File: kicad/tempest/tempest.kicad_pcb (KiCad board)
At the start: 2 copper layers, 300 x 300 mm, 18 parts

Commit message: Draw every device at its real package size
The board maps existed to answer "which chip is at C4", and then drew a
24-pin ROM and a 20-pin LS245 as the same 14-pin outline. package_for()
read pin counts from DEVICES, which holds 20 Pong-era parts against the
112 part types the boards actually use, and silently fell back to DIP-14
for the other 92.

tools/packages.py is the pin-count table, kept separate from devices.py
on purpose: packaging needs one number for every part on every board,
while devices.py carries verified pinouts for the parts validate_nets.py
reasons about, and widening that set to satisfy a drawing would let the
extractor trust readings nothing has checked.

688 of 704 devices now size. check_packages.py re-derives 56 of the
entries from KiCAD's symbol library — comparing the highest pin number,
not the pin count, since KiCAD omits no-connects and a 7493 symbol has
ten pins on a DIP-14 — and confirms all 20 parts in DEVICES agree. The
Am2901 slices and the POKEY come from DIP-40 stated on the Battlezone
sheet; the 8316E from the drawing's note that a 2708 may be fitted
instead.

What does not size is now said out loud rather than quietly drawn at 14
pins: four descriptions recorded where the sheet gave no part number,
and the Atari 0351xx ROM/PROM numbers, which get the class default and
are listed as unverified until someone has a board in front of them.

Two things found while reading the corpus for packages, both logged in
asteroids.read.json rather than acted on. The -06 rate multiplier
resolution was recorded and never applied to the board data, and the
parts list disagrees with both readings on designators. F4/H4/J4 take
either an LS670 or an LS170, and the 19-007 pull-up network is fitted
only with the LS170 — same package either way, but a real failure mode.

Also: republishing a board without --machine used to unlink it from its
machine, because most definitions carry no machine of their own and the
link lived only in boards.json. publish_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
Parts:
- UC4, UD10: footprint DIP-14_W7.62mm -> DIP-16_W7.62mm
- UK11: footprint DIP-14_W7.62mm -> DIP-8_W7.62mm
- UM12, UN12, UR9: footprint DIP-14_W7.62mm -> DIP-20_W7.62mm

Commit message: Drop two grid rows that do not exist, and span the devices that do
Atari's grid alphabet skips G, I, O and Q, and the board definitions
listed G and Q as rows. Every device below F was therefore drawn a row
too low, the rendered board carried two empty bands, and F/H1 looked
like a three-position span for a part 1.2in long on a 0.75in pitch.

Confirmed three ways before touching it. Nothing in any read, signature
or signal record in this repo sits in a G or Q row, while both
neighbours of each are populated on the two densest boards — Battlezone
P:6 R:2, Asteroids-03 P:4 R:3. The sheets' own spanning designators
treat F and H as adjacent and H and J as adjacent, which is only
possible if G and I are not positions. And with G removed, F/H falls out
as an adjacent pair, which is what a 24-pin ROM needs. Pong predates the
convention and legitimately uses G, so it keeps its grid.

Spans are now data rather than prose. A device drawn across two or three
cells is still keyed at its first cell, because that is the only thing
`ics` may be keyed by, but the sheet's own designator goes in a `spans`
map and the footprint is placed at the mean of the cells it names. A
DIP-40 at B/C2 sits between B2 and C2 instead of hanging equally over A2
and C2. The build rejects a span whose rows are not adjacent — that
failure almost always means the grid is wrong, not the span.

Two more inconsistencies found and logged rather than guessed at. Two of
the Math Box's four Am2901 slices carry a span and two do not, though
all four are the same DIP-40 on the same pitch. And asteroids-04.json
carries five devices at the -03 PROM positions alongside the -04 ROMs
and is missing 035144-02 at D/E1, contradicting the substitution table,
memory_by_revision and its own status text in the same breath.

Co-Authored-By: Claude Opus 5 <noreply@anthropic.com>
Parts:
- moved UA4 38.1 mm to (102.2, 265.6)
- moved UA6 38.1 mm to (153.0, 265.6)
- moved UE6 38.1 mm to (153.0, 189.4)
- moved UB4 38.1 mm to (102.2, 246.6)
- moved UD10 38.1 mm to (254.6, 208.5)
- moved UD4 38.1 mm to (102.2, 208.5)
- moved UF3 38.1 mm to (76.8, 170.4)
- moved UC4 38.1 mm to (102.2, 227.6)
- moved UK11 19.1 mm to (280.0, 113.2)
- moved UK9 19.1 mm to (229.2, 113.2)
- moved UN12 19.1 mm to (305.4, 56.1)
- moved UN13 19.1 mm to (330.8, 56.1)
- moved UN6 19.1 mm to (153.0, 56.1)
- moved UL12 19.0 mm to (305.4, 94.2)
- moved UL6 19.0 mm to (153.0, 94.2)
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
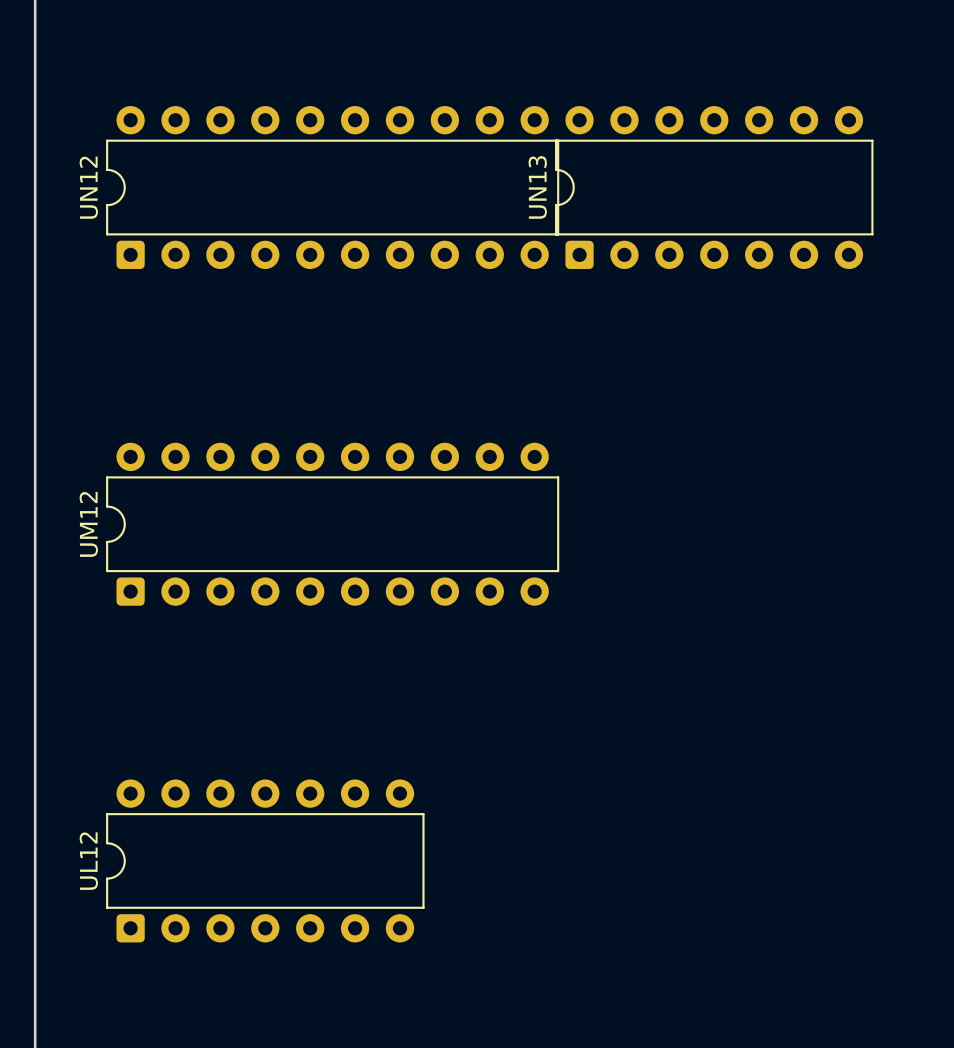
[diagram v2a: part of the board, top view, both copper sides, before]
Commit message: Name the four parts the sheets never did
C5, E12 and M12 on Asteroids were recorded by function — "counter",
"op-amp", "DIP switch" — because the drawings give no part number for
them, and they were the last devices the board maps could not size. The
parts lists give all three, and agree across printings.

C5 is a 9316. Five printings name a counter there: the 6th, 7th and
Cocktail 3rd say 37-9316, the 1st and 2nd say 37-74LS161, and the 9316
is Fairchild's 74161, so those are the same part and not a conflict. It
matches the read's own note that C5 divides 3kHz by 12 for the NMI.

E12 is Atari 137108-001, item 130, "Operational Amplifier Integrated
Circuit", at E12 in three printings; the Caberat manual names the type,
TL081CP. Same designator, same block, three documents. The same item
also lists a B/C12 location that nothing in the read accounts for, which
is noted and not acted on.

M12 is Atari 66-114P1T, a 4-station DIP switch, item 143 at M12 in three
printings. Sized as DIP-8, since n SPST switches in a DIP is 2n pins;
the 8-station switches on Battlezone and Tempest are DIP-16 for the same
reason.

All three are cross-document confirmations rather than re-readings of
the same sheet, which is the route the house rules say to try first and
the one that has resolved every conflict here so far. Every device on
every board now has a package: 106 of 106 part types, 694 of 694
devices. What remains unverified is the twenty Atari 0351xx ROM/PROM
positions, drawn on a class default, and those want a board.

Co-Authored-By: Claude Opus 5 <noreply@anthropic.com>
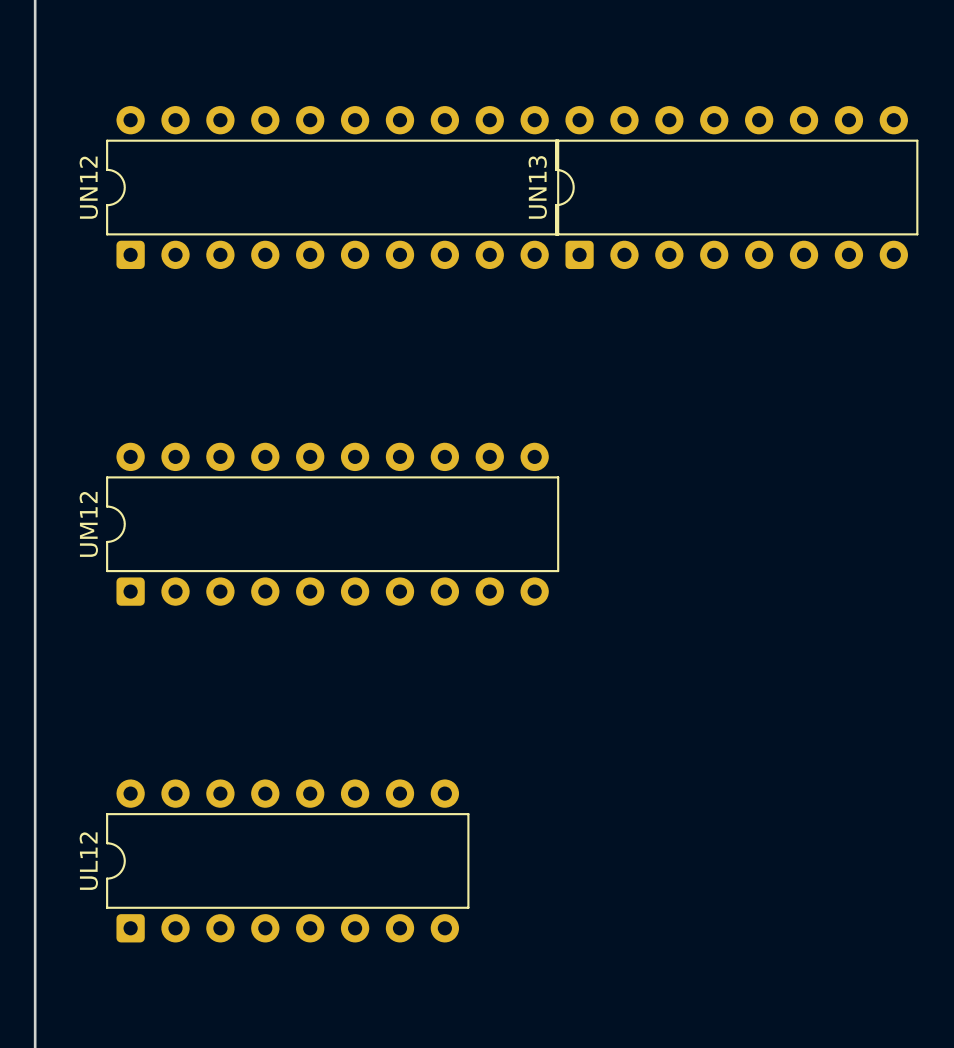
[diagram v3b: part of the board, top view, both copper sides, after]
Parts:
- UL12, UN13: footprint DIP-14_W7.62mm -> DIP-16_W7.62mm

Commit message: Unlock Centipede and Tempest on a hyphen
Checking whether mikesarcade.com had anything this corpus lacks turned
up something better: Centipede and Tempest harvested nothing at all,
from forty-six and thirty-seven documents each, while Asteroids and
Battlezone gave up eighty to a hundred designators apiece. Same
manufacturer, same era, same parts-list format.

The difference was one character. Asteroids writes 'Type 74LS04
Integrated Circuit (B5)'; Centipede and Tempest write 'Type-74LS04'. The
type pattern required whitespace, so those rows never matched, fell
through to the count layout, found no leading quantity, and were
discarded silently.

Centipede goes from 23 devices to 87, Tempest from 18 to 83. Both
agree with themselves across every printing with no split, and both
confirm every drawing device the lists also name. Tempest needs
--figure: its manual carries an Auxiliary PCB alongside the
vector-generator board, and only the latter has a map.

Two more readings resolved against the drawing, on the same evidence as
Missile Command's D3. Centipede M4 is a 74LS175, not a 74LS75 — nine
printings, and 75 against 175 is a dropped digit. Tempest L6 is a
74LS670, not a 74LS14: four printings put it in a bank of three register
files at K6, L6 and M6, which is the same trio Asteroids has at F4, H4
and J4 on the same vector generator, so the grouping is coherent as well
as attested.

74LS373 and the CD4584B join the packaging table. 1,461 devices across
27 boards, all sized, none contradicted by a socket entry.

Co-Authored-By: Claude Opus 5 <noreply@anthropic.com>
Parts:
- added UA1: 74LS244, DIP-20_W7.62mm, F.Cu at (26.0, 256.1)
- added UA7: 74LS02, DIP-14_W7.62mm, F.Cu at (178.4, 265.6)
- added UA8: 74LS109, DIP-16_W7.62mm, F.Cu at (203.8, 265.6)
- added UA9: 74LS164, DIP-14_W7.62mm, F.Cu at (229.2, 265.6)
- added UB1: 74LS244, DIP-20_W7.62mm, F.Cu at (26.0, 237.1)
- added UB3: 74LS139, DIP-16_W7.62mm, F.Cu at (76.8, 246.6)
- added UB5: 74LS02, DIP-14_W7.62mm, F.Cu at (127.6, 246.6)
- added UB6: 74LS27, DIP-14_W7.62mm, F.Cu at (153.0, 246.6)
- added UB7: 74S74, DIP-14_W7.62mm, F.Cu at (178.4, 246.6)
- added UB8: 74LS74, DIP-14_W7.62mm, F.Cu at (203.8, 246.6)
- added UB9: 74LS32, DIP-14_W7.62mm, F.Cu at (229.2, 246.6)
- added UC1: 74LS139, DIP-16_W7.62mm, F.Cu at (26.0, 227.6)
- added UC3: 74LS32, DIP-14_W7.62mm, F.Cu at (76.8, 227.6)
- added UC5: 74S260, DIP-14_W7.62mm, F.Cu at (127.6, 227.6)
- added UC6: 74S02, DIP-14_W7.62mm, F.Cu at (153.0, 227.6)
- added UC7: 74S74, DIP-14_W7.62mm, F.Cu at (178.4, 227.6)
- added UC8: 74LS161, DIP-16_W7.62mm, F.Cu at (203.8, 227.6)
- added UD3: 74LS74, DIP-14_W7.62mm, F.Cu at (76.8, 208.5)
- added UD5: 74LS194, DIP-16_W7.62mm, F.Cu at (127.6, 208.5)
- added UD6: 74LS194, DIP-16_W7.62mm, F.Cu at (153.0, 208.5)
- added UD8: 74LS161, DIP-16_W7.62mm, F.Cu at (203.8, 208.5)
- added UD9: 74LS273, DIP-20_W7.62mm, F.Cu at (229.2, 208.5)
- added UE2: 74LS244, DIP-20_W7.62mm, F.Cu at (51.4, 189.4)
- added UE3: 74S04, DIP-14_W7.62mm, F.Cu at (76.8, 189.4)
- added UE4: 74LS161, DIP-16_W7.62mm, F.Cu at (102.2, 189.4)
- added UE5: 74LS194, DIP-16_W7.62mm, F.Cu at (127.6, 189.4)
- added UE7: 74LS174, DIP-16_W7.62mm, F.Cu at (178.4, 189.4)
- added UE8: 74LS161, DIP-16_W7.62mm, F.Cu at (203.8, 189.4)
- added UE9: 74LS20, DIP-14_W7.62mm, F.Cu at (229.2, 189.4)
- added UF2: 74LS245, DIP-20_W7.62mm, F.Cu at (51.4, 170.4)
- added UF4: 74LS10, DIP-14_W7.62mm, F.Cu at (102.2, 170.4)
- added UF5: 74LS194, DIP-16_W7.62mm, F.Cu at (127.6, 170.4)
- added UF6: 74S00, DIP-14_W7.62mm, F.Cu at (153.0, 170.4)
- added UF7: 74LS42, DIP-16_W7.62mm, F.Cu at (178.4, 170.4)
- added UF8: 74LS161, DIP-16_W7.62mm, F.Cu at (203.8, 170.4)
- added UH2: 74LS245, DIP-20_W7.62mm, F.Cu at (51.4, 151.3)
- added UH3: 74LS245, DIP-20_W7.62mm, F.Cu at (76.8, 151.3)
- added UH5: 74LS194, DIP-16_W7.62mm, F.Cu at (127.6, 151.3)
- added UH6: 74LS194, DIP-16_W7.62mm, F.Cu at (153.0, 151.3)
- added UH7: 74LS175, DIP-16_W7.62mm, F.Cu at (178.4, 151.3)
- added UH8: 74LS174, DIP-16_W7.62mm, F.Cu at (203.8, 151.3)
- added UH9: 74LS399, DIP-16_W7.62mm, F.Cu at (229.2, 151.3)
- added UJ2: 74LS139, DIP-16_W7.62mm, F.Cu at (51.4, 132.3)
- added UJ5: 74LS139, DIP-16_W7.62mm, F.Cu at (127.6, 132.3)
- added UJ6: 74LS191, DIP-16_W7.62mm, F.Cu at (153.0, 132.3)
- added UJ7: 74LS175, DIP-16_W7.62mm, F.Cu at (178.4, 132.3)
- added UJ8: 74LS32, DIP-14_W7.62mm, F.Cu at (203.8, 132.3)
- added UK2: 74LS157, DIP-16_W7.62mm, F.Cu at (51.4, 113.2)
- added UK5: 74LS193, DIP-16_W7.62mm, F.Cu at (127.6, 113.2)
- added UK6: 74LS670, DIP-16_W7.62mm, F.Cu at (153.0, 113.2)
- added UK7: 74LS367, DIP-16_W7.62mm, F.Cu at (178.4, 113.2)
- added UK8: 74LS175, DIP-16_W7.62mm, F.Cu at (203.8, 113.2)
- added UL2: 74LS157, DIP-16_W7.62mm, F.Cu at (51.4, 94.2)
- added UL5: 74LS193, DIP-16_W7.62mm, F.Cu at (127.6, 94.2)
- added UL8: 74LS191, DIP-16_W7.62mm, F.Cu at (203.8, 94.2)
- added UM2: 74LS157, DIP-16_W7.62mm, F.Cu at (51.4, 75.2)
- added UM5: 74LS193, DIP-16_W7.62mm, F.Cu at (127.6, 75.2)
- added UM6: 74LS670, DIP-16_W7.62mm, F.Cu at (153.0, 75.2)
- added UN2: 74LS157, DIP-16_W7.62mm, F.Cu at (51.4, 56.1)
- added UN7: 74LS367, DIP-16_W7.62mm, F.Cu at (178.4, 56.1)
- added UN8: 74LS174, DIP-16_W7.62mm, F.Cu at (203.8, 56.1)
- added UN9: 74LS174, DIP-16_W7.62mm, F.Cu at (229.2, 56.1)
- added UP7: 74LS139, DIP-16_W7.62mm, F.Cu at (178.4, 37.0)
- added UP8: 74LS157, DIP-16_W7.62mm, F.Cu at (203.8, 37.0)
- added UR7: 74LS32, DIP-14_W7.62mm, F.Cu at (178.4, 18.0)
- UL6: value 74LS14 -> 74LS670; footprint DIP-14_W7.62mm -> DIP-16_W7.62mm

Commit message: Place the memory devices the IC parts lists cannot reach
Atari stocks ROM, RAM and the microprocessor under its own part numbers
— 90-7033, 036175-01, 90-6013 — not as 37-series IC stock, so the IC
harvest cannot see them however well it reads. That is why Centipede's
ROMs were missing and Red Baron's map had ten devices. merge_memory.py
reads those rows from the same typeset parts lists, under the same rules
as the IC merge: the drawing wins where it exists, two documents must
agree, and nothing is placed whose package cannot be established.

Red Baron 10 to 15, Asteroids Deluxe 92 to 100, Tempest 83 to 88,
Centipede 93 to 95, Missile Command 83 to 85, Lunar Lander 60 to 62.
1,494 devices across the boards, all sized, none contradicted.

Establishing the packages took two corrections, and both were the same
mistake in different clothes.

The first attempt sized Atari stock numbers by correlating a part
against the contact count of the socket at the positions it occupies,
pooled across a machine's documents. That is not a near miss: it put the
2114 at 40 pins, on twelve positions of apparent evidence, because two
printings number the board differently and the correlation was reading
one printing's parts list against another's sockets. Confined to within
a single document it behaves — 33 stock numbers established, 90-6013 by
39 documents agreeing, and 90-7033 correctly refusing to answer rather
than answering wrongly. Those 33 are in packages.py with their
provenance.

The second was the same shape. MAME's dump size was sizing a part from
whatever MAME dumped at that cell, which on Red Baron meant sizing
036175-01 from a dump of 037000-01 — sizing the socket, not the chip.
MAME now sizes a part only when the dump is of that part. Red Baron
loses two devices and keeps thirteen that are right.

Four more parts are sized from MAME's dump sizes alone, where every set
carrying the part agrees and the era leaves no room: 32 bytes and 256
bytes are both bipolar PROMs in a 1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
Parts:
- added UC2: 90-6013, DIP-40_W15.24mm, F.Cu at (51.4, 227.6)
- added UD1: 136002-101, DIP-24_W15.24mm, F.Cu at (26.0, 208.5)
- added UD7: 136002-125, DIP-16_W7.62mm, F.Cu at (178.4, 208.5)
- added UN3: 136002-111, DIP-24_W15.24mm, F.Cu at (76.8, 46.6)
- added UR3: 136002-112, DIP-24_W15.24mm, F.Cu at (76.8, 18.0)
